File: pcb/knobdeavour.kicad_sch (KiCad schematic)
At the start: 99 parts, among them J0 USB_C_Receptacle_USB2.0, J1 BREAKOUT, J2 Conn_01x03_Male, J4 Conn_01x01_Male, K1 KEYSW, K10 KEYSW, K11 KEYSW, K12 KEYSW, K13 KEYSW, K14 KEYSW, K15 KEYSW, K16 KEYSW, K17 KEYSW, K18 KEYSW, K19 KEYSW, K2 KEYSW, K20 KEYSW, K21 KEYSW, K22 KEYSW, K23 KEYSW, K24 KEYSW, K25 KEYSW, K26 KEYSW, K27 KEYSW, K28 KEYSW, K29 KEYSW, K3 KEYSW, K30 KEYSW, K31 KEYSW, K32 KEYSW, K33 KEYSW, K34 KEYSW, K35 KEYSW, K36 KEYSW, K37 KEYSW, K38 KEYSW, K39 KEYSW, K4 KEYSW, K40 KEYSW, K41 KEYSW, K5 KEYSW, K6 KEYSW, K7 KEYSW, K8 KEYSW, K9 KEYSW, SW1 RotaryEncoder_Switch, SW2 RotaryEncoder_Switch, SW3 SW_PUSH, SW4 RESET, U1 NCP1117-3.3_SOT223, U2 W25Q128JVS, U3 RP2040, U44 SRV05-4, Y0 12MHZ Crystal

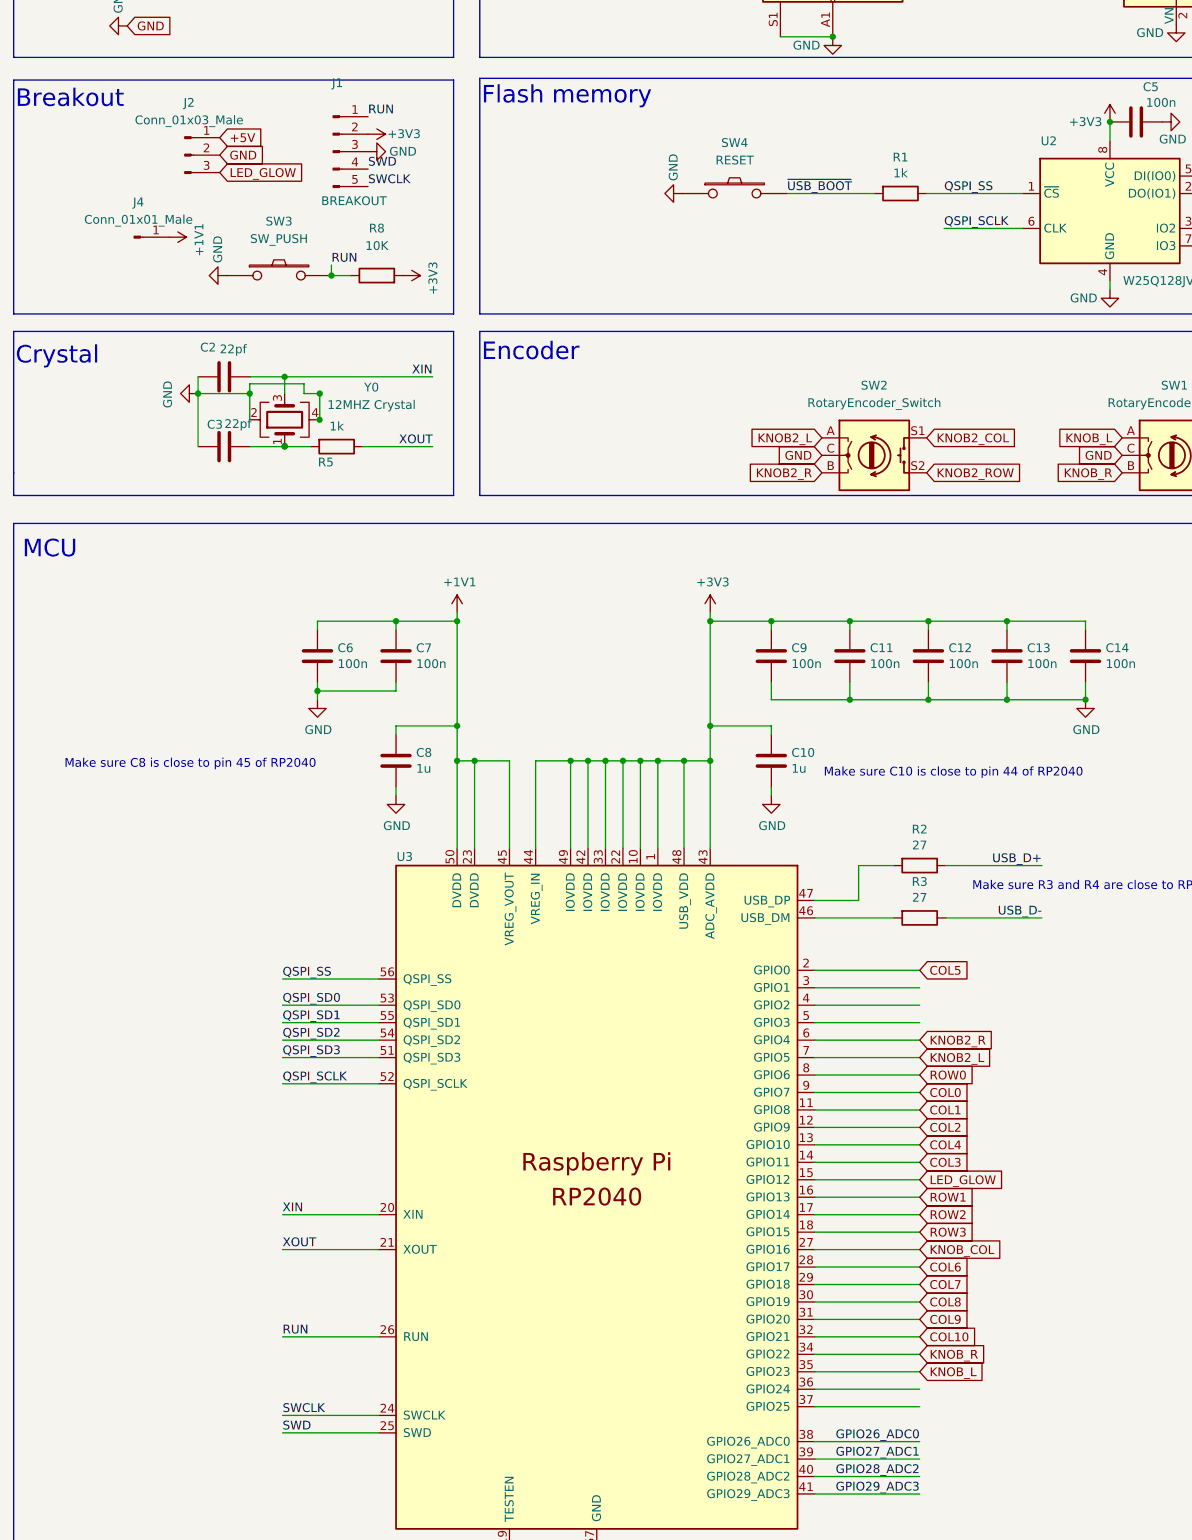
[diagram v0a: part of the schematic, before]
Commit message: updated Pcb and production files.
- added two additional breakouts for GPIO pins > next to Encoder
- replaced pin-breakout for Leds with larger 2.54mm pin-sockets for
  easier soldering
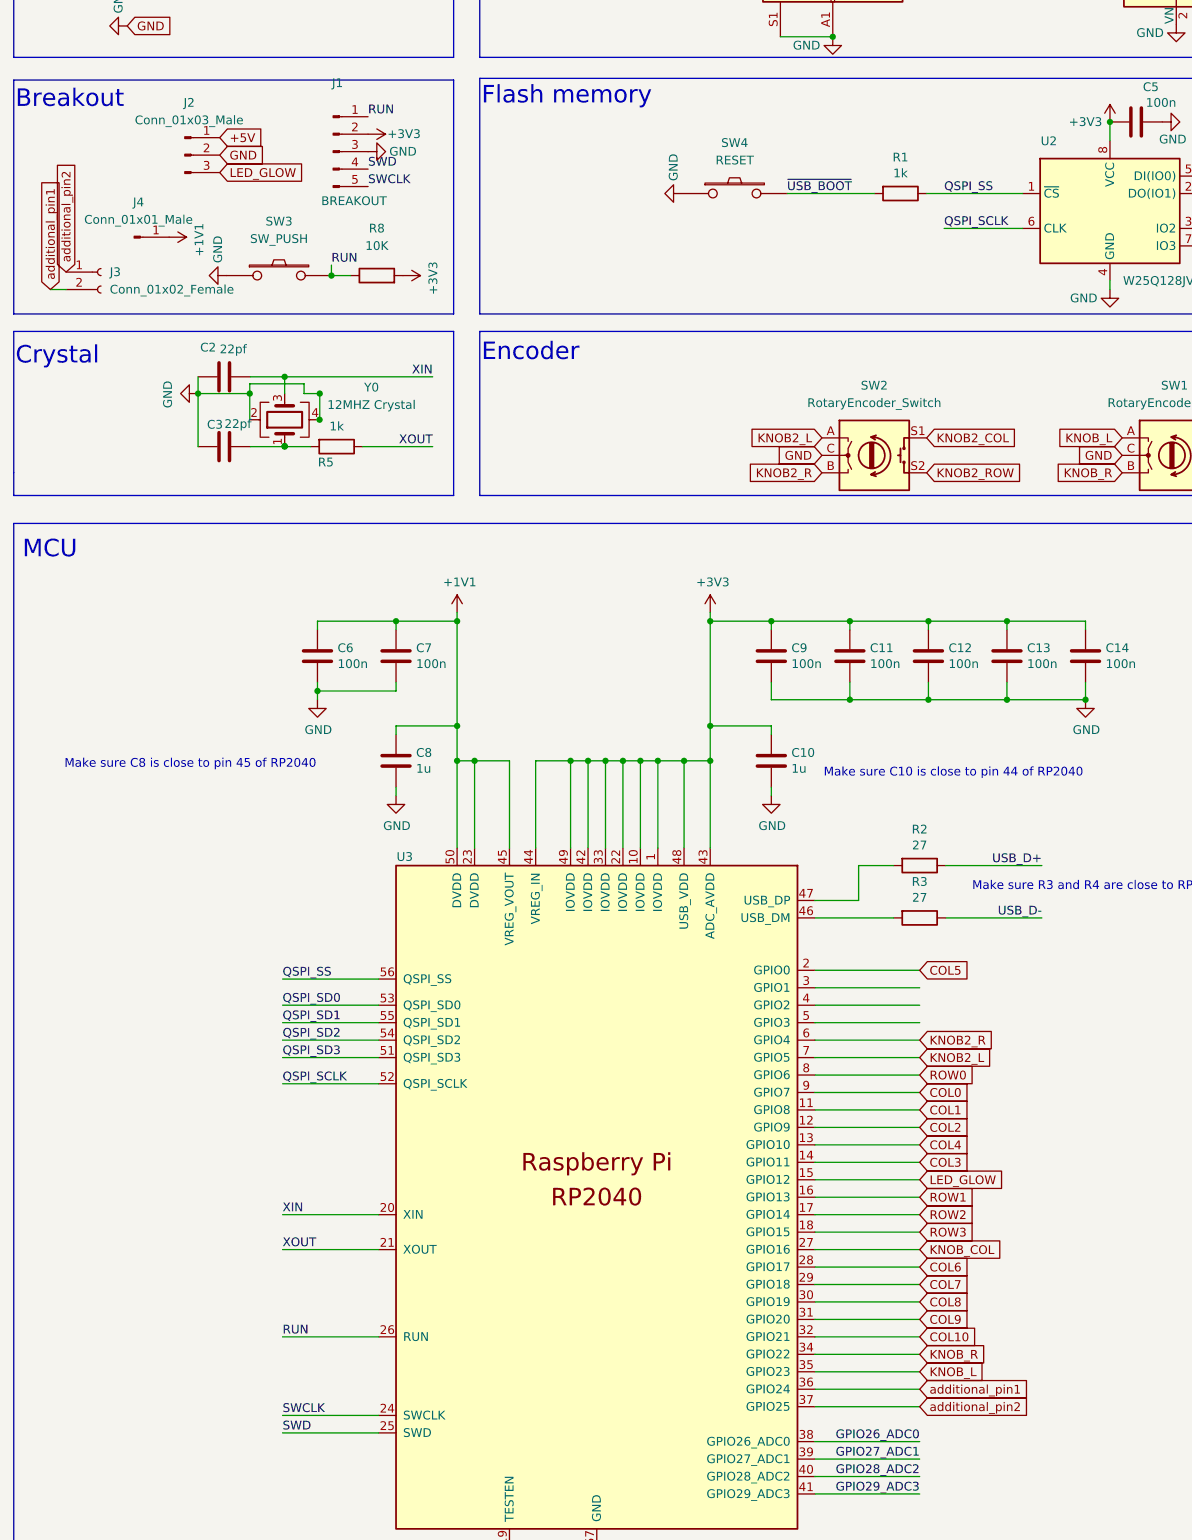
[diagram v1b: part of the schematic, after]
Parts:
- added J3: Conn_01x02_Female, Connector_PinSocket_2.54mm:PinSocket_1x02_P2.54mm_Vertical, symbol Connector:Conn_01x02_Female
- J2: footprint Connector_PinSocket_1.27mm:PinSocket_1x03_P1.27mm_Vertical -> Connector_PinSocket_2.54mm:PinSocket_1x03_P2.54mm_Vertical
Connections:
- net additional_pin1: now reaches U3.36 (GPIO24)
- net additional_pin1: now also J3.2 (Pin_2)
- net additional_pin2: now reaches U3.37 (GPIO25)
- net additional_pin2: now also J3.1 (Pin_1)
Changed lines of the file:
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@@
     (stroke (width 0) (type default) (color 0 0 0 0))
   )
+  (wire (pts (xy 19.304 210.566) (xy 21.59 210.566))
+    (stroke (width 0) (type default) (color 0 0 0 0))
+  )
   (wire (pts (xy 130.556 347.726) (xy 145.796 347.726))
     (stroke (width 0) (type default) (color 0 0 0 0))
@@
     )
   )
+  (global_label "additional_pin2" (shape input) (at 145.796 373.126 0) (fields_autoplaced)
+    (effects (font (size 1.27 1.27)) (justify left))
+    (property "Intersheet References" "${INTERSHEET_REFS}" (id 0) (at 162.7839 373.0466 0)
+      (effects (font (size 1.27 1.27)) (justify left) hide)
+    )
+  )
   (global_label "COL2" (shape input) (at 145.796 332.486 0) (fields_autoplaced)
     (effects (font (size 1.27 1.27)) (justify left))
@@
     )
   )
+  (global_label "additional_pin1" (shape input) (at 19.304 210.566 90) (fields_autoplaced)
+    (effects (font (size 1.27 1.27)) (justify left))
+    (property "Intersheet References" "${INTERSHEET_REFS}" (id 0) (at 19.2246 193.5781 90)
+      (effects (font (size 1.27 1.27)) (justify left) hide)
+    )
+  )
   (global_label "COL10" (shape input) (at 145.796 362.966 0) (fields_autoplaced)
     (effects (font (size 1.27 1.27)) (justify left))
@@
     )
   )
+  (global_label "additional_pin2" (shape input) (at 21.59 208.026 90) (fields_autoplaced)
+    (effects (font (size 1.27 1.27)) (justify left))
+    (property "Intersheet References" "${INTERSHEET_REFS}" (id 0) (at 21.5106 191.0381 90)
+      (effects (font (size 1.27 1.27)) (justify left) hide)
+    )
+  )
   (global_label "KNOB2_ROW" (shape input) (at 146.812 237.236 0) (fields_autoplaced)
     (effects (font (size 1.27 1.27)) (justify left))
@@
     )
   )
+  (global_label "additional_pin1" (shape input) (at 145.796 370.586 0) (fields_autoplaced)
+    (effects (font (size 1.27 1.27)) (justify left))
+    (property "Intersheet References" "${INTERSHEET_REFS}" (id 0) (at 162.7839 370.5066 0)
+      (effects (font (size 1.27 1.27)) (justify left) hide)
+    )
+  )
   (global_label "COL9" (shape input) (at 486.918 295.148 90) (fields_autoplaced)
     (effects (font (size 1.27 1.27)) (justify left))
@@
     (property "Reference" "J2" (id 0) (at 39.497 183.388 0))
     (property "Value" "Conn_01x03_Male" (id 1) (at 39.497 185.928 0))
-    (property "Footprint" "Connector_PinSocket_1.27mm:PinSocket_1x03_P1.27mm_Vertical" (id 2) (at 38.862 191.008 0)
+    (property "Footprint" "Connector_PinSocket_2.54mm:PinSocket_1x03_P2.54mm_Vertical" (id 2) (at 38.862 191.008 0)
       (effects (font (size 1.27 1.27)) hide)
     )
@@
     (pin "2")
   )
+  (symbol (lib_id "Connector:Conn_01x02_Female") (at 26.67 208.026 0) (unit 1)
+    (in_bom yes) (on_board yes) (fields_autoplaced)
+    (property "Reference" "J3" (id 0) (at 27.94 208.0259 0)
+      (effects (font (size 1.27 1.27)) (justify left))
+    )
+    (property "Value" "Conn_01x02_Female" (id 1) (at 27.94 210.5659 0)
+      (effects (font (size 1.27 1.27)) (justify left))
+    )
+    (property "Footprint" "Connector_PinSocket_2.54mm:PinSocket_1x02_P2.54mm_Vertical" (id 2) (at 26.67 208.026 0)
+      (effects (font (size 1.27 1.27)) hide)
+    )
+    (property "Datasheet" "~" (id 3) (at 26.67 208.026 0)
+      (effects (font (size 1.27 1.27)) hide)
+    )
+    (pin "1")
+    (pin "2")
+  )
   (sheet_instances
     (path "/" (page "1"))
@@
     )
     (path "/d1c8f35c-2f81-44c3-92ac-c2b939a3237a"
-      (reference "J2") (unit 1) (value "Conn_01x03_Male") (footprint "Connector_PinSocket_1.27mm:PinSocket_1x03_P1.27mm_Vertical")
+      (reference "J2") (unit 1) (value "Conn_01x03_Male") (footprint "Connector_PinSocket_2.54mm:PinSocket_1x03_P2.54mm_Vertical")
+    )
+    (path "/ff75ac43-7a8e-495d-b7ce-dc18a6170443"
+      (reference "J3") (unit 1) (value "Conn_01x02_Female") (footprint "Connector_PinSocket_2.54mm:PinSocket_1x02_P2.54mm_Vertical")
     )
     (path "/e4a9861a-d787-47b8-b6cf-05f988622a5d"
